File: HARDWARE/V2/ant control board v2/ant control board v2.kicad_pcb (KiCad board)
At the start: 2 copper layers, 22.8 x 33.2 mm, 97 parts, among them J1 B_SW, J10 M2, J11 M3, J2 2s Battery, J4 USB-C_304A-ACP16X, J5 custom analog 2, J6 custom analog 1, J7 servo 2, J8 servo 1 (HV), J9 M1, SW1 BOOT, SW2 RESET, U1 TPS563200, U10 AT24C02C, U2 STM32F070CBTx, U3 H7233-1, U4 FS2A 4CH reciever, U5 DRV8838, U6 DRV8838, U7 DRV8838, U8 74LVC1T45DW-7, U9 74LVC1T45DW-7, Y1 TAXM8M4RLBDDT2T

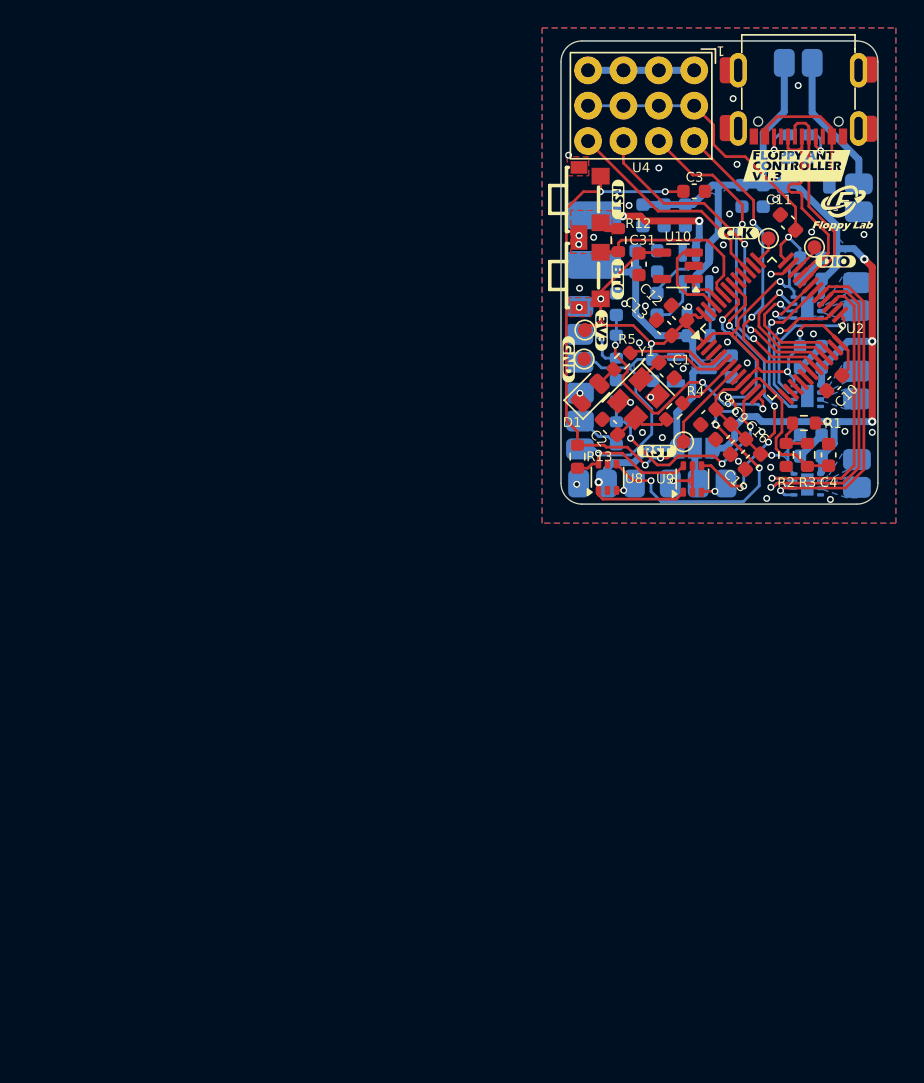
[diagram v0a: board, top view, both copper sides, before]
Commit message: layout 2.0 facv2 done
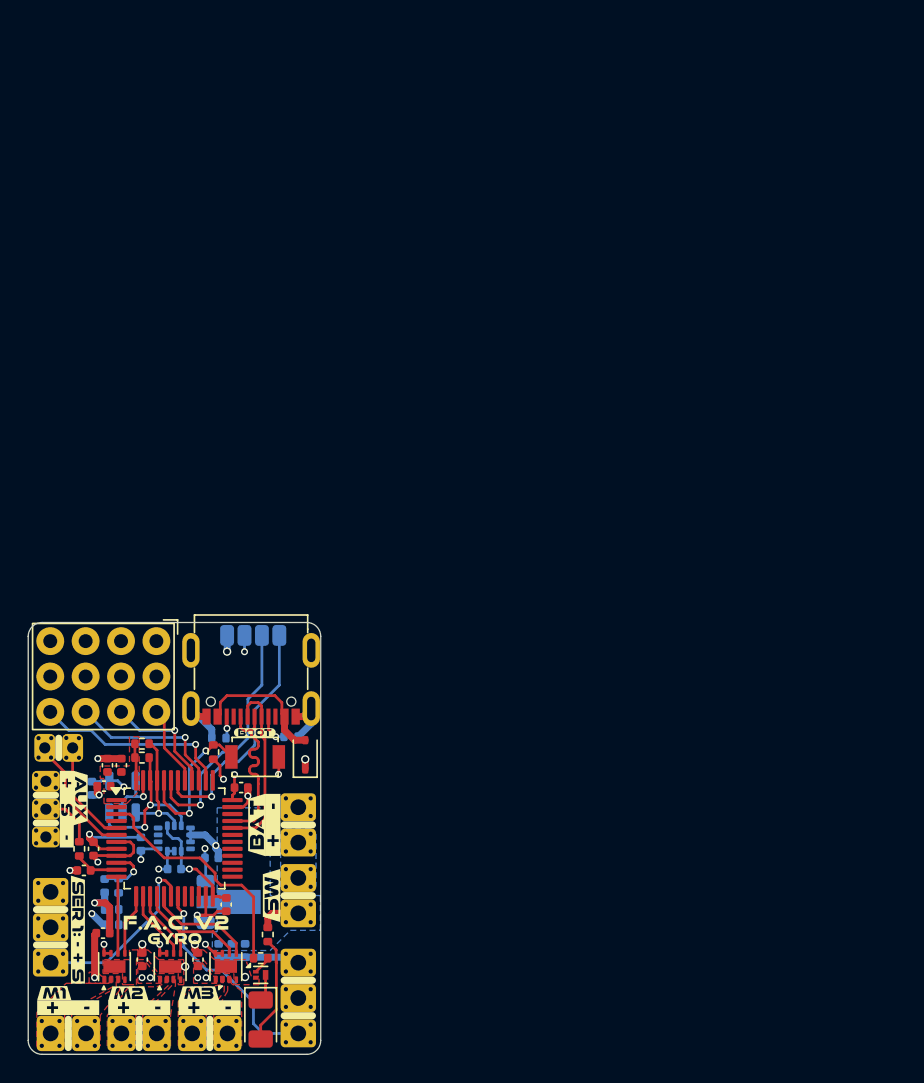
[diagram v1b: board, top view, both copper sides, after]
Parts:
- removed C12, C20, C21, C25, C26, C27, C28, C29, C30, C31: 100n, Capacitor_SMD:C_0603_1608Metric
- removed C22: 22u, Capacitor_SMD:C_0603_1608Metric
- removed C23, C24: 4.7u, Capacitor_SMD:C_0603_1608Metric
- removed J11: M3, _MY_connectors:Pad 02x01
- removed JP1: SERVO2 PW, Jumper:SolderJumper-3_P1.3mm_Open_RoundedPad1.0x1.5mm_NumberLabels
- removed L1: 4.7uH, _My_inductors:XRCD43-3R3M
- removed R12, R13: 5.1k, Resistor_SMD:R_0603_1608Metric
- removed SW2: RESET, _MIA footprint:SW-SMD_TS24CA SMD BUTTO 90deg
- removed TP1: RST, TestPoint:TestPoint_Pad_D1.0mm
- removed TP2: SWDIO, TestPoint:TestPoint_Pad_D1.0mm
- removed TP3: SWCLK, TestPoint:TestPoint_Pad_D1.0mm
- removed TP4: 3V3, TestPoint:TestPoint_Pad_D1.0mm
- removed TP5: GND, TestPoint:TestPoint_Pad_D1.0mm
- removed U10: AT24C02C, Package_TO_SOT_SMD:SOT-23-5
- removed U9: 74LVC1T45DW-7, Package_TO_SOT_SMD:SOT-363_SC-70-6
- removed Y1: TAXM8M4RLBDDT2T, Crystal:Crystal_SMD_3225-4Pin_3.2x2.5mm
- removed kibuzzard-667D9F03: G***, kibuzzard-667D9F03
- removed kibuzzard-667D9F0F: G***, kibuzzard-667D9F0F
- removed kibuzzard-667D9F19: G***, kibuzzard-667D9F19
- removed kibuzzard-667D9F22: G***, kibuzzard-667D9F22
- removed kibuzzard-667D9F2A: G***, kibuzzard-667D9F2A
- removed kibuzzard-667D9F56: G***, kibuzzard-667D9F56
- removed kibuzzard-667D9F7E: G***, kibuzzard-667D9F7E
- removed kibuzzard-667D9F87: G***, kibuzzard-667D9F87
- removed kibuzzard-667D9F8D: G***, kibuzzard-667D9F8D
- removed kibuzzard-667D9F91: G***, kibuzzard-667D9F91
- removed kibuzzard-667D9F97: G***, kibuzzard-667D9F97
- removed kibuzzard-667D9FA0: G***, kibuzzard-667D9FA0
- removed kibuzzard-667D9FA9: G***, kibuzzard-667D9FA9
- removed kibuzzard-667D9FAD: G***, kibuzzard-667D9FAD
- removed kibuzzard-667D9FB5: G***, kibuzzard-667D9FB5
- removed kibuzzard-669B8939: G***, kibuzzard-669B8939
- removed kibuzzard-669B8C44: G***, kibuzzard-669B8C44
- removed kibuzzard-66A643AC: G***, kibuzzard-66A643AC
- removed kibuzzard-66A6444D: G***, kibuzzard-66A6444D
- removed kibuzzard-66AE2B42: G***, kibuzzard-66AE2B42
- added J12: ELRS, _MY_connectors:Pad 01x04 small, B.Cu at (117.0, 110.9)
- added J3: USB-C_304A-ACP16X, _MIA footprint:USB_C_304A-ACP16X, F.Cu at (115.0, 112.0)
- added Q1: NMOS, Package_DFN_QFN:Diodes_DFN1006-3, F.Cu at (115.7, 135.3)
- added kibuzzard-68CD6E18: G***, kibuzzard-68CD6E18, F.Cu at (116.5, 129.6)
- added kibuzzard-68CD6E18: G***, kibuzzard-68CD6E18, B.Cu at (116.5, 129.6)
- added kibuzzard-68CD6E40: G***, kibuzzard-68CD6E40, F.Cu at (107.0, 137.7)
- added kibuzzard-68CD6E40: G***, kibuzzard-68CD6E40, F.Cu at (101.9, 137.7)
- added kibuzzard-68CD6E40: G***, kibuzzard-68CD6E40, F.Cu at (116.6, 124.5)
- added kibuzzard-68CD6E40: G***, kibuzzard-68CD6E40, F.Cu at (112.0, 137.7)
- added kibuzzard-68CD6E53: G***, kibuzzard-68CD6E53, F.Cu at (115.4, 124.5)
- added kibuzzard-68CD6E53: G***, kibuzzard-68CD6E53, B.Cu at (115.4, 124.5)
- added kibuzzard-68CD717E: G***, kibuzzard-68CD717E, F.Cu at (102.6, 132.1)
- added kibuzzard-68CD71AA: G***, kibuzzard-68CD71AA, F.Cu at (100.9, 136.6)
- added kibuzzard-68CD71AA: G***, kibuzzard-68CD71AA, B.Cu at (102.9, 136.6)
- added kibuzzard-68CD7254: G***, kibuzzard-68CD7254, F.Cu at (106.2, 136.6)
- added kibuzzard-68CD7254: G***, kibuzzard-68CD7254, B.Cu at (107.8, 136.6)
- added kibuzzard-68CD725D: G***, kibuzzard-68CD725D, F.Cu at (111.2, 136.6)
- added kibuzzard-68CD725D: G***, kibuzzard-68CD725D, B.Cu at (112.8, 136.6)
- added kibuzzard-68CD73CB: G***, kibuzzard-68CD73CB, F.Cu at (102.8, 122.6)
- added kibuzzard-68CD73D1: G***, kibuzzard-68CD73D1, F.Cu at (101.8, 123.4)
- added kibuzzard-68CD7457: G***, kibuzzard-68CD7457, F.Cu at (115.3, 117.9)
- added kibuzzard-68CD756A: G***, kibuzzard-68CD756A, B.Cu at (116.6, 124.5)
- added kibuzzard-68CD75CA: G***, kibuzzard-68CD75CA, B.Cu at (107.0, 137.6)
- added kibuzzard-68CD75CA: G***, kibuzzard-68CD75CA, B.Cu at (112.0, 137.6)
- added kibuzzard-68CD75CA: G***, kibuzzard-68CD75CA, B.Cu at (101.9, 137.6)
- added kibuzzard-68CD7642: G***, kibuzzard-68CD7642, B.Cu at (103.5, 131.9)
- added kibuzzard-68CD769D: G***, kibuzzard-68CD769D, B.Cu at (115.6, 136.9)
- added kibuzzard-68CD76C6: G***, kibuzzard-68CD76C6, B.Cu at (102.5, 131.9)
- added kibuzzard-68CD784B: G***, kibuzzard-68CD784B, B.Cu at (116.6, 136.9)
- added kibuzzard-68CD787F: G***, kibuzzard-68CD787F, B.Cu at (102.7, 123.4)
- added kibuzzard-68CD78A4: G***, kibuzzard-68CD78A4, B.Cu at (101.8, 123.4)
- added kibuzzard-68CD78BE: G***, kibuzzard-68CD78BE, B.Cu at (105.7, 118.7)
- added kibuzzard-68CD78F0: G***, kibuzzard-68CD78F0, B.Cu at (105.8, 119.7)
- added kibuzzard-68CD793B: G***, kibuzzard-68CD793B, B.Cu at (113.2, 113.4)
- added kibuzzard-68CD795A: G***, kibuzzard-68CD795A, B.Cu at (114.5, 113.4)
- added kibuzzard-68CD79A4: G***, kibuzzard-68CD79A4, B.Cu at (117.0, 113.4)
- added kibuzzard-68CD79BE: G***, kibuzzard-68CD79BE, B.Cu at (115.8, 113.4)
- added kibuzzard-68CD7A1F: G***, kibuzzard-68CD7A1F, B.Cu at (115.1, 115.4)
- added kibuzzard-68CD7AD1: G***, kibuzzard-68CD7AD1, B.Cu at (113.6, 120.5)
- added kibuzzard-68CD7AF2: G***, kibuzzard-68CD7AF2, F.Cu at (109.6, 131.6)
- added kibuzzard-68CD7CD9: G***, kibuzzard-68CD7CD9, F.Cu at (109.5, 132.7)
- added kibuzzard-68CD7CD9: G***, kibuzzard-68CD7CD9, B.Cu at (109.8, 121.9)
- C1, C2: value 20p -> 4.7u; footprint Capacitor_SMD:C_0603_1608Metric -> Capacitor_SMD:C_0402_1005Metric; moved to B.Cu
- C10, C4, C8, C9: footprint Capacitor_SMD:C_0603_1608Metric -> Capacitor_SMD:C_0402_1005Metric; moved to B.Cu
- C11, C16: footprint Capacitor_SMD:C_0603_1608Metric -> Capacitor_SMD:C_0402_1005Metric
- C13: value 100n -> 4.7u; footprint Capacitor_SMD:C_0603_1608Metric -> Capacitor_SMD:C_0402_1005Metric
- C14: footprint Capacitor_SMD:C_0603_1608Metric -> Capacitor_SMD:C_0402_1005Metric; moved to F.Cu
- C15, C19: value 4.7u -> 100n; footprint Capacitor_SMD:C_0603_1608Metric -> Capacitor_SMD:C_0402_1005Metric
- C17, C18: value 22u -> 100n; footprint Capacitor_SMD:C_0603_1608Metric -> Capacitor_SMD:C_0402_1005Metric; moved to F.Cu
- C3: value 100n -> 4.7u; footprint Capacitor_SMD:C_0603_1608Metric -> Capacitor_SMD:C_0402_1005Metric; moved to B.Cu
- C5, C6: value 22u -> 4.7u; footprint Capacitor_SMD:C_0603_1608Metric -> Capacitor_SMD:C_0402_1005Metric; moved to F.Cu
- C7: value 100n -> 4.7u; footprint Capacitor_SMD:C_0603_1608Metric -> Capacitor_SMD:C_0402_1005Metric; moved to F.Cu
- D1: value STATUS -> 1N5819WS; footprint LED_SMD:LED_0805_2012Metric -> Diode_SMD:D_SOD-323
- D2: value SD103AW -> STATUS; footprint Diode_SMD:D_SOD-123 -> LED_SMD:LED_1206_3216Metric; moved to F.Cu
- G***: moved to B.Cu
- J1: value B_SW -> SWITCH; footprint _MY_connectors:Pad 02x01 -> _MY_connectors:01x02_TH_pad_renforced; moved to F.Cu
- J10: value M2 -> DIGITAL_AUX; footprint _MY_connectors:Pad 02x01 -> _MY_connectors:01x02_TH_pad_renforced_small; moved to F.Cu
- J2: footprint _MY_connectors:Pad 02x01 -> _MY_connectors:01x02_TH_pad_renforced; moved to F.Cu
- J4: value USB-C_304A-ACP16X -> M1; footprint _MIA footprint:USB_C_304A-ACP16X -> _MY_connectors:01x02_TH_pad_renforced
- J5: value custom analog 2 -> M2; footprint _MY_connectors:Pad 03x01 -> _MY_connectors:01x02_TH_pad_renforced; moved to F.Cu
- J6: value custom analog 1 -> M3; footprint _MY_connectors:Pad 03x01 -> _MY_connectors:01x02_TH_pad_renforced; moved to F.Cu
- J7: value servo 2 -> servo 1; footprint _MY_connectors:Pad 03x01 -> _MY_connectors:01x03_TH_pad_renforced; moved to F.Cu
- J8: value servo 1 (HV) -> servo 2; footprint _MY_connectors:Pad 03x01 -> _MY_connectors:01x03_TH_pad_renforced; moved to F.Cu
- J9: value M1 -> ADC_AUX; footprint _MY_connectors:Pad 02x01 -> _MY_connectors:01x03_TH_pad_renforced_small; moved to F.Cu
- R1: value 10k -> 5.1k; footprint Resistor_SMD:R_0603_1608Metric -> Resistor_SMD:R_0402_1005Metric; moved to B.Cu
- R10, R8, R9: footprint Resistor_SMD:R_0603_1608Metric -> Resistor_SMD:R_0402_1005Metric; moved to F.Cu
- R11: value 5.1k -> 1.5k; footprint Resistor_SMD:R_0603_1608Metric -> Resistor_SMD:R_0402_1005Metric; moved to F.Cu
- R2, R3: footprint Resistor_SMD:R_0603_1608Metric -> Resistor_SMD:R_0402_1005Metric; moved to B.Cu
- R4: value 1k -> 1.5k; footprint Resistor_SMD:R_0603_1608Metric -> Resistor_SMD:R_0402_1005Metric; moved to B.Cu
- R5: value 5.1k -> 10k; footprint Resistor_SMD:R_0603_1608Metric -> Resistor_SMD:R_0402_1005Metric; moved to B.Cu
- R6: value 54.9k -> 5.1k; footprint Resistor_SMD:R_0603_1608Metric -> Resistor_SMD:R_0402_1005Metric; moved to F.Cu
- R7: value 10k -> 5.1k; footprint Resistor_SMD:R_0603_1608Metric -> Resistor_SMD:R_0402_1005Metric; moved to F.Cu
- SW1: footprint _MIA footprint:SW-SMD_TS24CA SMD BUTTO 90deg -> Button_Switch_SMD:SW_SPST_B3U-1000P
- U1: value TPS563200 -> GM7333; footprint Package_TO_SOT_SMD:SOT-23-6 -> Package_TO_SOT_SMD:SOT-89-3
- U2: value STM32F070CBTx -> DRV8837; footprint Package_QFP:LQFP-48_7x7mm_P0.5mm -> Package_SON:WSON-8-1EP_2x2mm_P0.5mm_EP0.9x1.6mm
- U3: value H7233-1 -> DRV8837; footprint Package_TO_SOT_SMD:SOT-23-3 -> Package_SON:WSON-8-1EP_2x2mm_P0.5mm_EP0.9x1.6mm; moved to F.Cu
- U4: value FS2A 4CH reciever -> DRV8837; footprint _My_modules:FS2A 4CH reciever -> Package_SON:WSON-8-1EP_2x2mm_P0.5mm_EP0.9x1.6mm
- U5: value DRV8838 -> LSM6DS3; footprint Package_SON:WSON-8-1EP_2x2mm_P0.5mm_EP0.9x1.6mm -> Package_LGA:LGA-14_3x2.5mm_P0.5mm_LayoutBorder3x4y
- U6: value DRV8838 -> STM32F072CBTx; footprint Package_SON:WSON-8-1EP_2x2mm_P0.5mm_EP0.9x1.6mm -> Package_QFP:LQFP-48_7x7mm_P0.5mm; moved to F.Cu
- U7: value DRV8838 -> FS2A 4CH reciever; footprint Package_SON:WSON-8-1EP_2x2mm_P0.5mm_EP0.9x1.6mm -> _My_modules:FS2A 4CH reciever; moved to F.Cu
- U8: value 74LVC1T45DW-7 -> AT24C02C; footprint Package_TO_SOT_SMD:SOT-363_SC-70-6 -> Package_TO_SOT_SMD:SOT-23-5; moved to B.Cu
- moved J4 87.5 mm to (100.6, 139.5), turned to 0 degrees
- moved U4 72.6 mm to (113.2, 134.7), turned to 90 degrees
- moved G*** 72.1 mm to (108.3, 132.8), turned to 180 degrees
- moved D2 71.6 mm to (115.7, 138.5), turned to -90 degrees
- moved C11 68.7 mm to (103.0, 127.8), turned to 0 degrees
- moved J1 68.6 mm to (118.4, 128.3), turned to -90 degrees
- moved U2 65.8 mm to (105.2, 134.7), turned to 90 degrees
- moved C6 65.3 mm to (107.2, 134.2), turned to 90 degrees
- moved R8 64.9 mm to (107.2, 119.7), turned to 180 degrees
- moved C5 64.5 mm to (104.4, 132.3), turned to 0 degrees
- moved C3 64.3 mm to (112.7, 133.6), turned to -90 degrees
- moved C19 64.3 mm to (103.6, 121.9)
- moved C7 63.9 mm to (111.2, 134.2), turned to 90 degrees
- moved R9 63.2 mm to (107.2, 118.7), turned to 180 degrees
- moved J9 62.6 mm to (100.3, 121.4), turned to -90 degrees
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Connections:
- net /BAT_2_SW renamed /Power/+SW
- C1 pad 1: /OSC_IN -> +BATT
- C11 pad 1: +3V3 -> GND
- C11 pad 2: GND -> /MCU and RX/ADC1
- C14 pad 1: Net-(U1-VBST) -> +3V3
- C14 pad 2: /SW -> GND
- C17 pad 1: +5V -> +3V3
- C18 pad 1: +5V -> +3V3
- C19 pad 1: +BATT -> +3V3
- C2 pad 1: Net-(C2-Pad1) -> +BATT
- C3 pad 1: /RESET -> +BATT
- C4 pad 1: GND -> +3V3
- C4 pad 2: /VBAT -> GND
- C8 pad 1: +3V3 -> GND
- C8 pad 2: GND -> /MCU and RX/VBAT
- D1 pad 1: GND -> +BATT
- D1 pad 2: Net-(D1-A) -> /Power/VUSB
- D2 pad 1: +BATT -> Net-(D2-K)
- D2 pad 2: /VUSB -> Net-(D2-A)
- J10 pad 1: /M2+ -> /MCU and RX/DIGITAL_AUX1
- J10 pad 2: /M2- -> /MCU and RX/DIGITAL_AUX2
- J4 pad 1: GND -> /DC Motors/M1+
- J4 pad 2: /VUSB -> /DC Motors/M1-
- J5 pad 1: +3V3 -> /DC Motors/M2+
- J5 pad 2: Net-(J5-Pin_2) -> /DC Motors/M2-
- J6 pad 1: +3V3 -> /DC Motors/M3+
- J6 pad 2: Net-(J6-Pin_2) -> /DC Motors/M3-
- J7 pad 1: /SERVO_2_SIG_5V -> /MCU and RX/SERVO1
- J7 pad 2: +5V -> +BATT
- J8 pad 1: /SERVO_1_SIG_5V -> /MCU and RX/SERVO2
- J8 pad 2: Net-(J8-Pin_2) -> +BATT
- J9 pad 1: /M1+ -> +3V3
- J9 pad 2: /M1- -> Net-(J9-Pin_2)
- R1 pad 1: +BATT -> Net-(J3-CC2)
- R1 pad 2: /VBAT_DIV -> GND
- R10 pad 1: Net-(J5-Pin_2) -> /MCU and RX/STATUS_LED
- R10 pad 2: /ADC2 -> Net-(Q1-G)
- R11 pad 1: Net-(J6-Pin_2) -> Net-(D2-A)
- R11 pad 2: /ADC1 -> +BATT
- R2 pad 1: /VBAT_DIV -> Net-(J3-CC1)
- R3 pad 1: /VBAT_DIV -> +BATT
- R3 pad 2: /VBAT -> /Sensors/VBAT_DIV
- R4 pad 1: Net-(C2-Pad1) -> /Sensors/VBAT_DIV
- R4 pad 2: /OSC_OUT -> GND
- R5 pad 1: Net-(D1-A) -> /Sensors/VBAT_DIV
- R5 pad 2: Net-(U2-PC15) -> /MCU and RX/VBAT
- R6 pad 1: +5V -> Net-(J9-Pin_2)
- R6 pad 2: /VFB -> /MCU and RX/ADC1
- R7 pad 1: /VFB -> /MCU and RX/BOOT0
- R8 pad 1: /CC1 -> /MCU and RX/I2C1_SDA
- R8 pad 2: GND -> +3V3
- R9 pad 1: /CC2 -> /MCU and RX/I2C1_SCL
- R9 pad 2: GND -> +3V3
- SW1 pad 2: /BOOT0 -> /MCU and RX/BOOT0
- U1 pad 2: /SW -> +BATT
- U1 pad 3: +BATT -> +3V3
- U2 pad 1: +3V3 -> +BATT
- U2 pad 2: unconnected-(U2-PC13-Pad2) -> /DC Motors/M1+
- U2 pad 3: unconnected-(U2-PC14-Pad3) -> /DC Motors/M1-
- U2 pad 4: Net-(U2-PC15) -> GND
- U2 pad 5: /OSC_IN -> /DC Motors/PWM_M1_B
- U2 pad 6: /OSC_OUT -> /DC Motors/PWM_M1_F
- U2 pad 7: /RESET -> +3V3
- U2 pad 8: GND -> +3V3
- U2 pad 9: +3V3 -> GND
- U3 pad 1: GND -> +BATT
- U3 pad 2: +3V3 -> /DC Motors/M2+
- U3 pad 3: +5V -> /DC Motors/M2-
- U4 pad 1: GND -> +BATT
- U4 pad 2: +3V3 -> /DC Motors/M3+
- U4 pad 3: /CH1_PPM -> /DC Motors/M3-
- U4 pad 5: +3V3 -> /DC Motors/PWM_M3_B
- U4 pad 6: /CH2 -> /DC Motors/PWM_M3_F
- U4 pad 7: GND -> +3V3
- U4 pad 9: /CH3 -> GND
- U5 pad 1: +BATT -> GND
- U5 pad 2: /M1+ -> GND
- U5 pad 3: /M1- -> GND
- U5 pad 4: GND -> unconnected-(U5-INT1-Pad4)
- U5 pad 5: /M1_PWM -> +3V3
- U5 pad 6: /M1_DIR -> GND
- U5 pad 7: /~{M1_SLEEP} -> GND
- U5 pad 9: GND -> unconnected-(U5-INT2-Pad9)
- U6 pad 1: +BATT -> +3V3
- U6 pad 2: /M2+ -> unconnected-(U6-PC13-Pad2)
- U6 pad 3: /M2- -> /MCU and RX/STATUS_LED
- U6 pad 4: GND -> unconnected-(U6-PC15-Pad4)
- U6 pad 5: /M2_PWM -> /MCU and RX/DIGITAL_AUX1
- U6 pad 6: /M2_DIR -> /MCU and RX/DIGITAL_AUX2
- U6 pad 7: /~{M2_SLEEP} -> +3V3
- U6 pad 8: +3V3 -> GND
- U6 pad 9: GND -> +3V3
- U7 pad 1: +BATT -> GND
- U7 pad 2: /M3+ -> +3V3
- U7 pad 3: /M3- -> /MCU and RX/CH1_PPM
- U7 pad 5: /M3_PWM -> +3V3
- U7 pad 6: /M3_DIR -> /MCU and RX/CH2
- U7 pad 7: /~{M3_SLEEP} -> GND
- U7 pad 9: GND -> /MCU and RX/CH3
- U8 pad 1: +5V -> /MCU and RX/I2C1_SCL
- U8 pad 3: /SERVO_2_SIG_5V -> /MCU and RX/I2C1_SDA
- U8 pad 4: /SERVO_2_SIG -> +3V3
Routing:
- net +3V3: track 118.6 -> 34.5 mm, vias 8 -> 11
- net +BATT: track 77.2 -> 8.23 mm, vias 4 -> 7
- net /RESET: track 42.7 -> 0.00 mm, vias 4 -> 0
- net +5V: track 39.0 -> 0.00 mm, vias 1 -> 0
- net GND: track 20.6 -> 53.5 mm, vias 41 -> 16
- net /SERVO_2_SIG: track 32.5 -> 0.00 mm, vias 6 -> 0
- net /CH3: track 25.0 -> 0.00 mm, vias 2 -> 0
- net /CH2: track 23.7 -> 0.00 mm, vias 2 -> 0
- net /M1_DIR: track 23.6 -> 0.00 mm, vias 1 -> 0
- net /M1_PWM: track 23.6 -> 0.00 mm, vias 1 -> 0
- net /CH1_PPM: track 22.6 -> 0.00 mm, vias 2 -> 0
- net /~{M1_SLEEP}: track 21.6 -> 0.00 mm, vias 1 -> 0
- net /SERVO_1_SIG: track 21.2 -> 0.00 mm, vias 4 -> 0
- net /ADC2: track 19.0 -> 0.00 mm, vias 3 -> 0
- net /MCU and RX/UART2_RX: track 0.00 -> 18.0 mm, vias 0 -> 1
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- added copper zone on In2.Cu, net +3V3
- added copper zone on F.Cu, net +BATT
- added copper zone on In2.Cu, net +BATT
- added copper zone on F.Cu, net /DC Motors/M1+
- added copper zone on F.Cu, net /DC Motors/M1-
- added copper zone on F.Cu, net /DC Motors/M2+
- added copper zone on F.Cu, net /DC Motors/M2-
- added copper zone on F.Cu, net /DC Motors/M3+
- added copper zone on F.Cu, net /DC Motors/M3-
- added copper zone on B.Cu, net /Power/+SW
- added copper zone on In1.Cu, net GND
- removed copper zone on B.Cu, net +3V3
- removed copper zone on B.Cu, net +5V
- removed copper zone on B.Cu, net /M1+
- removed copper zone on B.Cu, net /M1-
- removed copper zone on B.Cu, net /M2+
- removed copper zone on B.Cu, net /M2-
- removed copper zone on B.Cu, net /M3+
- removed copper zone on B.Cu, net /M3-
- removed copper zone on B.Cu, net GND
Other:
- board size 22.8 x 33.2 mm -> 21 x 31 mm
- copper layers 2 -> 4
- board text removed: "1"
- board text removed: "2"
- board text removed: "3"
- board text removed: "4"
- board text removed: "S"

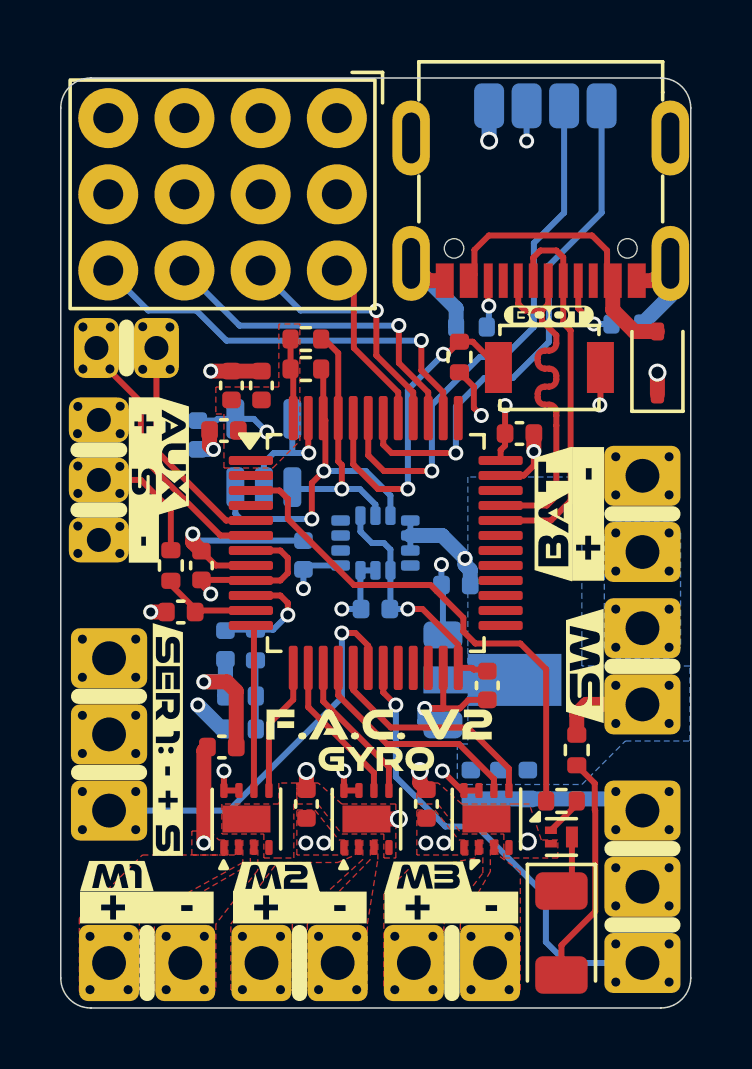
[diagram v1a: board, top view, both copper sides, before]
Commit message: adjusted some strace position and teardrops. Fixed silkscreedn
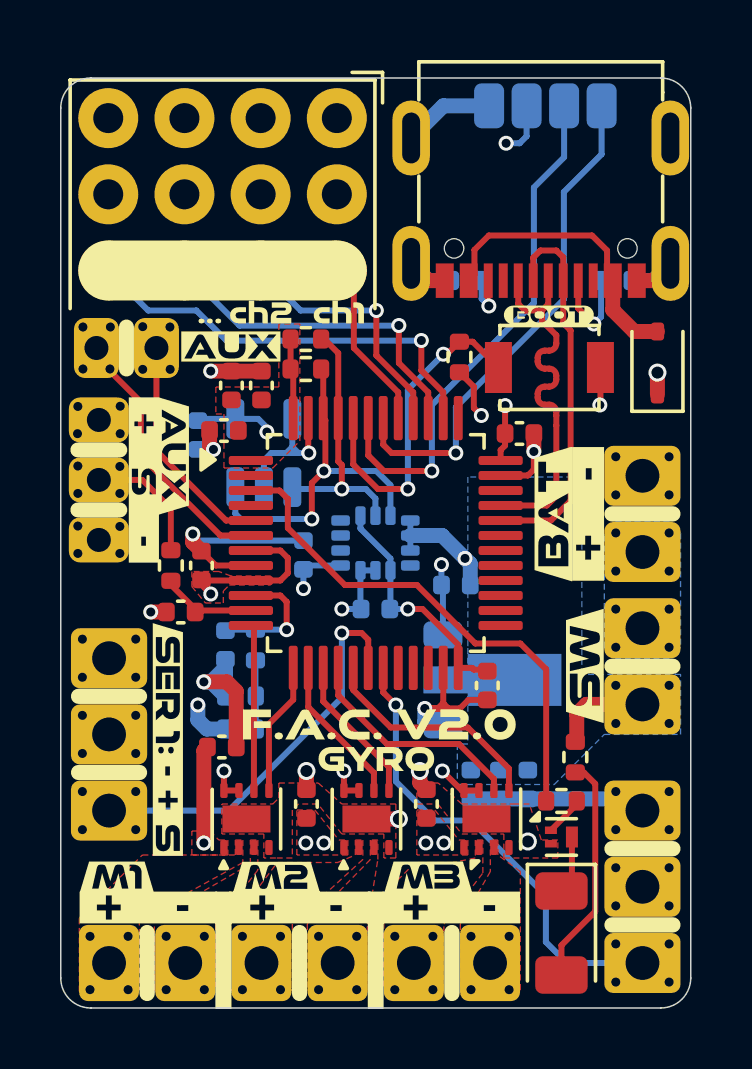
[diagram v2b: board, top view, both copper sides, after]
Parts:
- removed the kibuzzard-68CD6E40 at (107.0, 137.7)
- removed the kibuzzard-68CD6E40 at (101.9, 137.7)
- removed the kibuzzard-68CD6E40 at (112.0, 137.7)
- removed kibuzzard-68CD75CA (x3): G***, kibuzzard-68CD75CA
- removed kibuzzard-68CD76C6: G***, kibuzzard-68CD76C6
- removed kibuzzard-68CD7AD1: G***, kibuzzard-68CD7AD1
- removed kibuzzard-68CD7AF2: G***, kibuzzard-68CD7AF2
- added kibuzzard-68CFBDBE: G***, kibuzzard-68CFBDBE, F.Cu at (101.9, 137.6)
- added kibuzzard-68CFBDCF: G***, kibuzzard-68CFBDCF, F.Cu at (107.0, 137.7)
- added kibuzzard-68CFBDD6: G***, kibuzzard-68CFBDD6, F.Cu at (112.0, 137.7)
- added kibuzzard-68CFBE33: G***, kibuzzard-68CFBE33, F.Cu at (104.7, 119.0)
- added kibuzzard-68CFBFAF: G***, kibuzzard-68CFBFAF, F.Cu at (108.3, 117.8)
- added kibuzzard-68CFBFFE: G***, kibuzzard-68CFBFFE, F.Cu at (105.7, 117.8)
- added kibuzzard-68CFC012: G***, kibuzzard-68CFC012, F.Cu at (104.0, 118.1)
- added kibuzzard-68CFC153: G***, kibuzzard-68CFC153, B.Cu at (102.5, 131.9)
- added kibuzzard-68CFCF36: G***, kibuzzard-68CFCF36, B.Cu at (101.9, 137.6)
- added kibuzzard-68CFCF3D: G***, kibuzzard-68CFCF3D, B.Cu at (112.0, 137.6)
- added kibuzzard-68CFCF49: G***, kibuzzard-68CFCF49, B.Cu at (106.9, 137.6)
- added kibuzzard-68CFD0CD: G***, kibuzzard-68CFD0CD, F.Cu at (109.6, 131.6)
- added kibuzzard-68CFD0E9: G***, kibuzzard-68CFD0E9, B.Cu at (113.8, 120.2)
- added kibuzzard-68CFD180: G***, kibuzzard-68CFD180, B.Cu at (117.6, 119.0)
- moved R1 1.56 mm to (112.5, 116.8)
- moved R2 1.49 mm to (117.5, 116.8)
- moved G*** 0.69 mm to (108.2, 132.1)
- moved R11 0.24 mm to (116.2, 132.6)
- moved kibuzzard-68CD7CD9 0.10 mm to (109.9, 121.8)
- moved kibuzzard-68CD725D 0.08 mm to (112.9, 136.6)
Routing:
- net GND: track 53.5 -> 56.2 mm, vias 16 -> 15
- net Net-(J3-CC1): track 2.25 -> 3.21 mm
- net /MCU and RX/UART2_TX: track 17.6 -> 17.0 mm
- net +BATT: track 8.23 -> 8.78 mm

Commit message: Updated BOM, added some images
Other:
- board text added: "WayWayWay"

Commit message: Adjusted some pcb things and re generated Prouction files
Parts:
- removed kibuzzard-68CFD180: G***, kibuzzard-68CFD180
- added kibuzzard-6901144A: G***, kibuzzard-6901144A, B.Cu at (117.6, 119.0)
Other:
- board text added: "x"
- board text added: "y"
- board text added: "z"
